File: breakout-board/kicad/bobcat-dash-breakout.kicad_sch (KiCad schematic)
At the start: 184 parts, among them J1 TO PI (40-pin ribbon), J10 ADS1115 PWR/I2C, J11 LIGHTS, J12 COIL, J13 TILT, J14 TEMP PROBE, J15 ADS1115 INPUTS, J16 MAX98357A STEREO, J17 POD, J2 POWER IN, J3 TO 5V BUCK, J4 SWITCHES, J5 TACH, J6 FUEL, J7 HORN, J8 SILENCE, J9 MAX98357A MONO, Q1 IRLZ44N, Q2 IRF4905, Q3 BC547B, Q4 BC547B, Q5 IRLZ44N, U1 PC817, U10 PC817, U11 DS18B20, U4 PC817, U5 PC817, U6 CD4060BE, U7 PC817, U8 PC817, U9 PC817

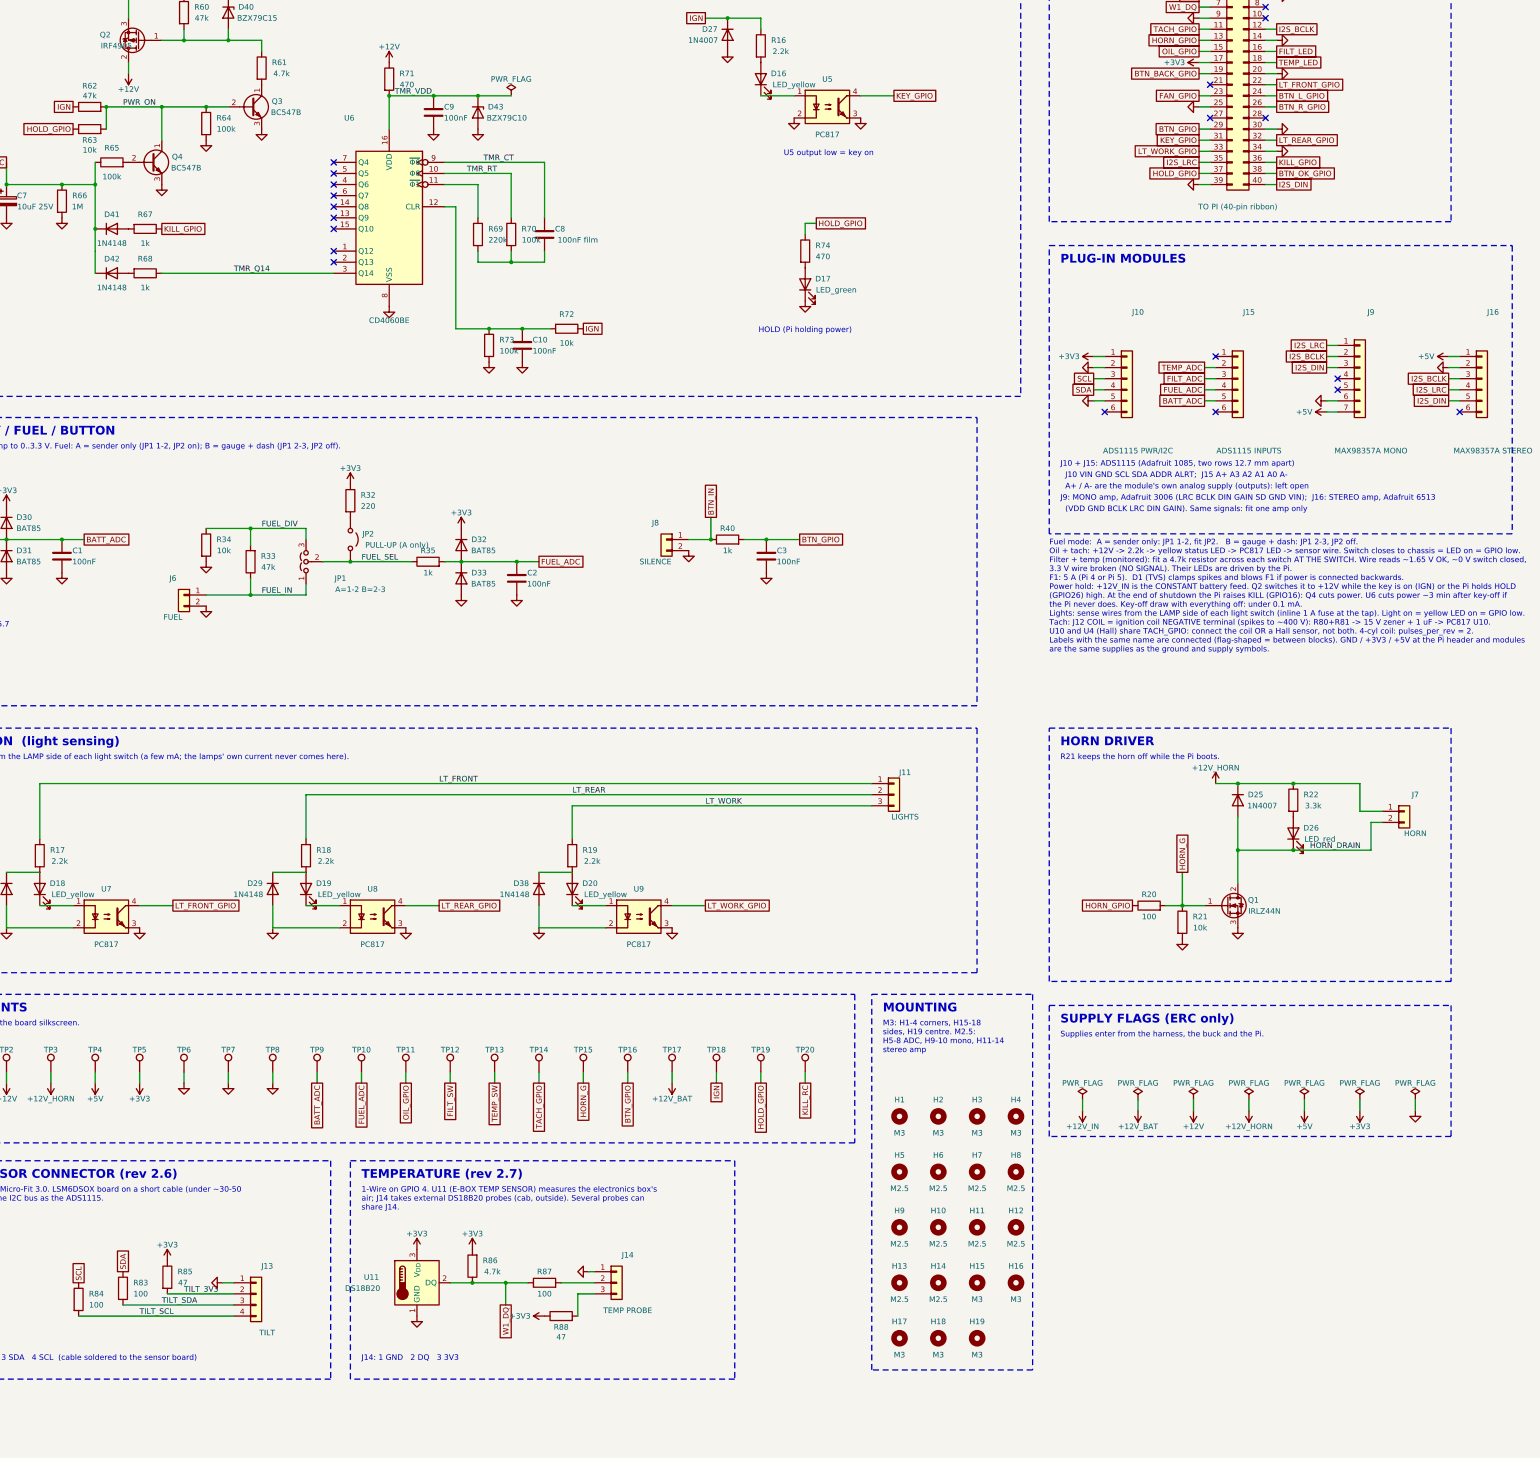
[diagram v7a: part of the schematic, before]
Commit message: Rev 3.0: cylinder head temps (CHT) and parking brake; new CHT + Parking Brake board
Software:
- cht.py: MCP9601 thermocouple amplifiers on I2C, per-cylinder limits
  (500 F warn, 550 F alarm + horn; factory head switches trip over 570 F),
  spread check vs the other cylinders' average, NO SIGNAL per cylinder.
  M.O.S.S. warns only, never stops the engine
- brake.py: (P) BRAKE tell-tale, PARKING BRAKE ON when working above idle
  with it set, SET PARKING BRAKE reminder at key-off
- Dash CYL HEAD TEMP tile, web Status tiles, Engine Status, alarm history,
  per-cylinder daily highs/lows in Reports; simulator keys ` and /
- [cht] and [park_brake] in config.toml (off until the hardware is fitted)

Breakout board rev 3.0:
- J18 AUX (Micro-Fit 2x3) to the CHT board: shared protected I2C,
  brake signal on GPIO 9 (R96 1k), brake LED feed from +12V (R97 2.2k)
- Routed, DRC and schematic parity clean; gerbers, BOM, renders, template

New breakout-board/cht-board (rev 1.0, 87 x 46 mm):
- Four sockets for Adafruit MCP9601 modules (address set by socket:
  0x60 / 0x65 / 0x66 / 0x67), parking brake optocoupler input, AUX plug
- Generator, KiCad project, gerbers, BOM, renders, README

BOM spreadsheet: CHT sensor, modules, Type K wire and connectors, brake switch

Co-Authored-By: Claude Opus 5.5 <noreply@anthropic.com>
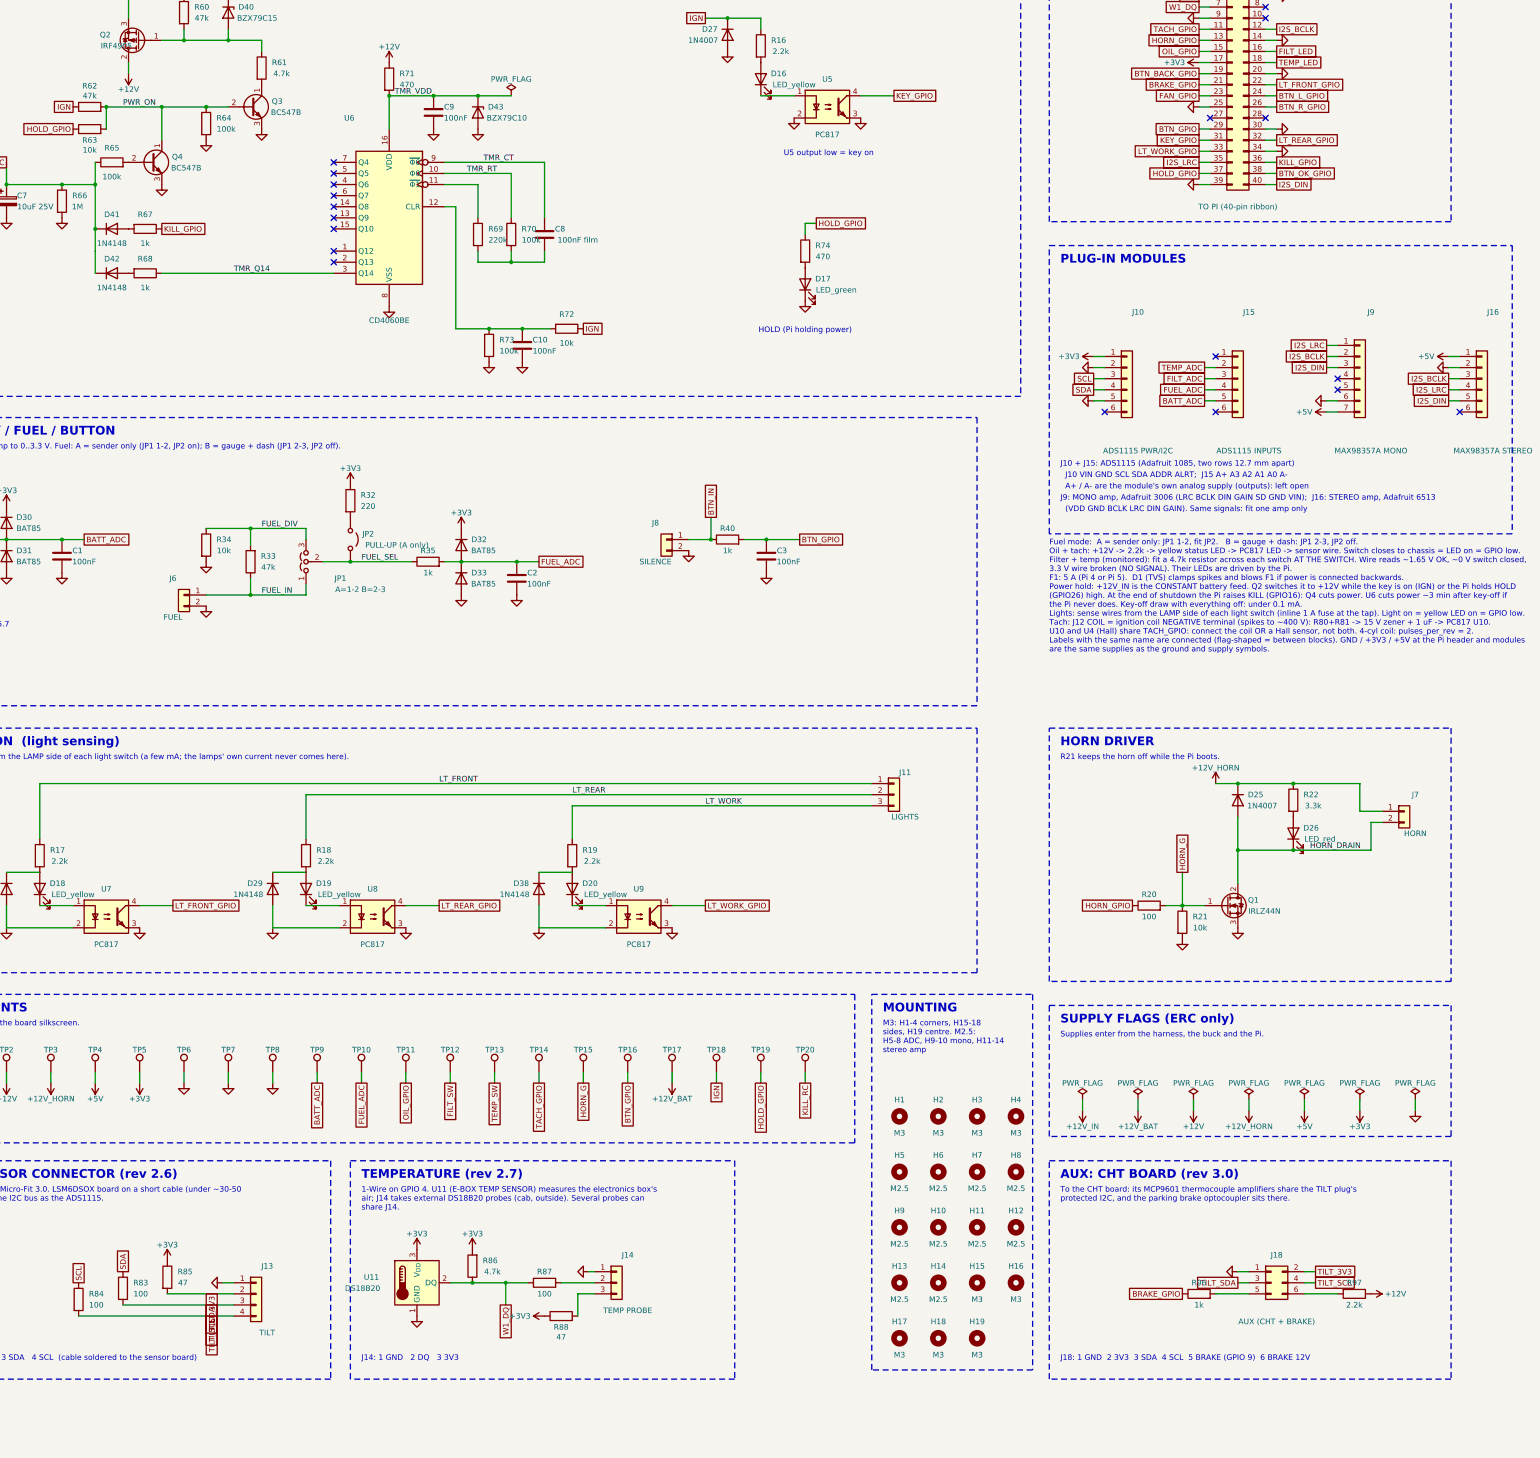
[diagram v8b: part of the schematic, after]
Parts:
- added J18: AUX (CHT + BRAKE), Connector_Molex:Molex_Micro-Fit_3.0_43045-0612_2x03_P3.00mm_Vertical, symbol Connector_Generic:Conn_02x03_Odd_Even
- added R96: 1k, Resistor_THT:R_Axial_DIN0207_L6.3mm_D2.5mm_P7.62mm_Horizontal, symbol Device:R
- added R97: 2.2k, Resistor_THT:R_Axial_DIN0207_L6.3mm_D2.5mm_P7.62mm_Horizontal, symbol Device:R
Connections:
- net +12V: now also R97.1
- net GND: now also J18.1 (Pin_1)
- net TILT_3V3: now also J18.2 (Pin_2)
- net TILT_SCL: now also J18.4 (Pin_4)
- net TILT_SDA: now also J18.3 (Pin_3)
- net BRAKE_GPIO: now reaches J1.21 (Pin_21)
- net BRAKE_GPIO: now also R96.1
- new net: J18.6 (Pin_6), R97.2
- new net: J18.5 (Pin_5), R96.2
- no-connect marks 20 -> 19
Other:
- note added: "AUX: CHT BOARD (rev 3.0)"
- note added: "J18: 1 GND 2 3V3 3 SDA 4 SCL 5 BRAKE (GPIO 9) 6 BRAKE 12V"
- note added: "To the CHT board: its MCP9601 thermocouple amplifiers share the TILT plug's protected I2C, and the parking brake optocoupler sits there."
